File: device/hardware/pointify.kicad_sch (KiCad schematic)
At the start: 14 parts, among them J1 USB_C, J2 SWIO, J3 GND, J4 PWM1, J5 PWM2, U1 CH32X033F8P6

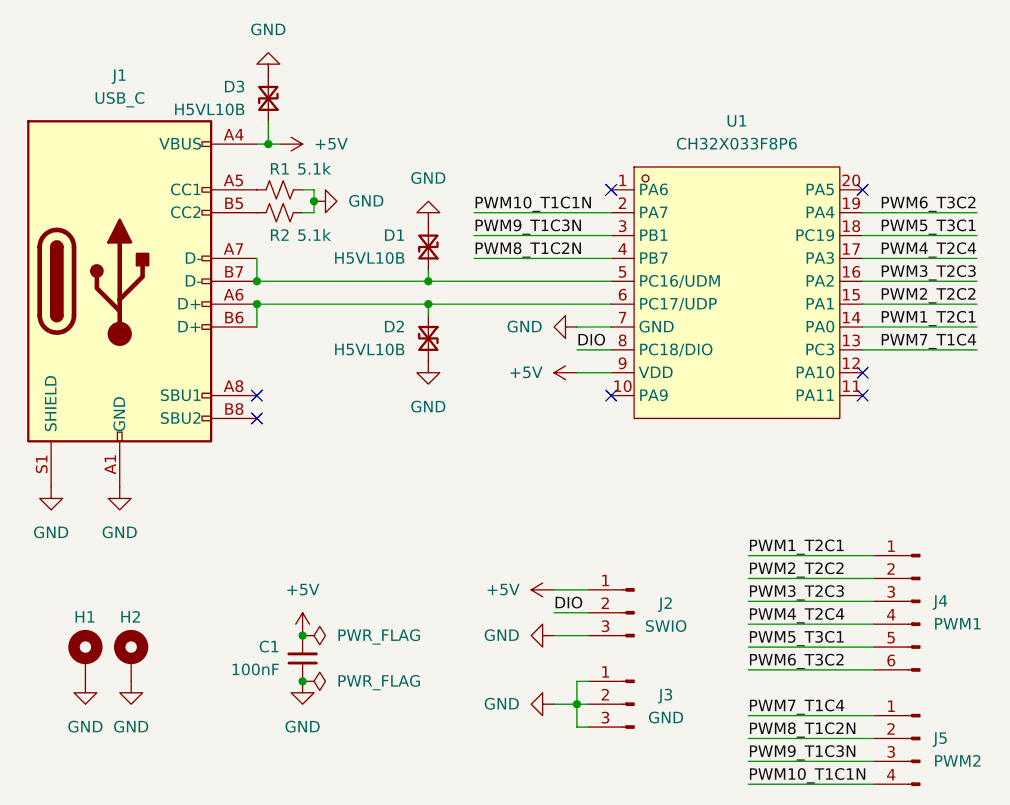
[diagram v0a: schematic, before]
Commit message: pcb v2.1: fix pinmaps
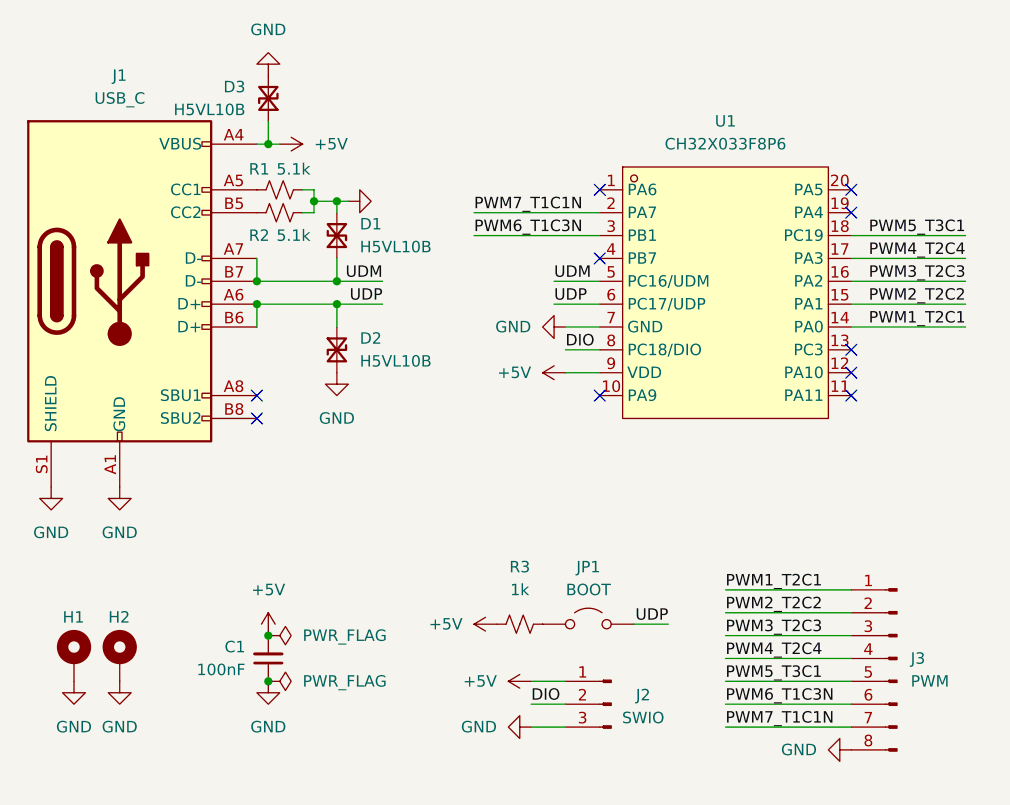
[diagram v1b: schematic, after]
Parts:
- removed J3: GND, Connector_PinHeader_2.54mm:PinHeader_1x03_P2.54mm_Vertical, symbol Connector:Conn_01x03_Pin
- removed J5: PWM2, Connector_PinHeader_2.00mm:PinHeader_1x04_P2.00mm_Vertical, symbol Connector:Conn_01x04_Pin
- added JP1: BOOT, Connector_PinHeader_2.54mm:PinHeader_1x02_P2.54mm_Vertical, symbol Jumper:Jumper_2_Open
- added R3: 1k, Resistor_SMD:R_0402_1005Metric_Pad0.72x0.64mm_HandSolder, symbol Device:R_Small_US
- J3: renamed from J4; value PWM1 -> PWM; footprint Connector_PinHeader_2.54mm:PinHeader_1x06_P2.54mm_Vertical -> Connector_PinHeader_2.54mm:PinHeader_1x08_P2.54mm_Vertical; symbol Connector:Conn_01x06_Pin -> Connector:Conn_01x08_Pin
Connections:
- net +5V: now also R3.1
- net GND: now also J3.8 (Pin_8)
- net UDP: now reaches D2.1 (A1), J1.A6 (D+), J1.B6 (D+), U1.6 (PC17/UDP)
- net UDP: now also JP1.2 (B)
- net UDM: now reaches D1.1 (A1), J1.A7 (D-), J1.B7 (D-), U1.5 (PC16/UDM)
- net PWM10_T1C1N renamed PWM7_T1C1N
- net PWM7_T1C1N: now also J3.7 (Pin_7)
- net PWM6_T3C2: no longer names the net of U1.19 (PA4)
- net PWM6_T3C2: no longer J3.6 (Pin_6)
- net PWM7_T1C4: no longer names the net of U1.13 (PC3)
- net PWM8_T1C2N: no longer names the net of U1.4 (PB7)
- net PWM9_T1C3N renamed PWM6_T1C3N
- net PWM6_T1C3N: now also J3.6 (Pin_6)
- new net: JP1.1 (A), R3.2
- no-connect marks 7 -> 10
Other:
- moved on the sheet: C1, D1, D2, H1, H2, J2, U1

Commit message: add: release workflows
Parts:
- H1, H2: now in the parts list
- J2, J3, JP1: now left out of the parts list
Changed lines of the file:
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@@
 		(unit 1)
 		(exclude_from_sim no)
-		(in_bom yes)
+		(in_bom no)
 		(on_board yes)
 		(dnp no)
@@
 		(unit 1)
 		(exclude_from_sim no)
-		(in_bom no)
+		(in_bom yes)
 		(on_board yes)
 		(dnp no)
@@
 		(unit 1)
 		(exclude_from_sim no)
-		(in_bom yes)
+		(in_bom no)
 		(on_board yes)
 		(dnp no)
@@
 		(unit 1)
 		(exclude_from_sim no)
-		(in_bom yes)
+		(in_bom no)
 		(on_board yes)
 		(dnp no)
@@
 		(unit 1)
 		(exclude_from_sim no)
-		(in_bom no)
-		(on_board yes)
-		(dnp no)
+		(in_bom yes)
+		(on_board yes)
+		(dnp no)

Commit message: update: pcb v2.2
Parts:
- removed D1, D2, D3: H5VL10B, Diode_SMD:D_SOD-882, symbol Device:D_TVS_Small
- removed J2: SWIO, Connector_PinHeader_2.54mm:PinHeader_1x03_P2.54mm_Vertical, symbol Connector:Conn_01x03_Pin
- added C2: 1uF, Capacitor_SMD:C_0402_1005Metric, symbol Device:C_Small
- C1: footprint Capacitor_SMD:C_0402_1005Metric_Pad0.74x0.62mm_HandSolder -> Capacitor_SMD:C_0402_1005Metric
- JP1: footprint Connector_PinHeader_2.54mm:PinHeader_1x02_P2.54mm_Vertical -> Connector_PinHeader_2.00mm:PinHeader_1x02_P2.00mm_Vertical
- R1, R2, R3: footprint Resistor_SMD:R_0402_1005Metric_Pad0.72x0.64mm_HandSolder -> Resistor_SMD:R_0402_1005Metric
- U1: footprint ch32x033f8p6:CH32X033F8P6 -> Package_SO:TSSOP-20_4.4x6.5mm_P0.65mm
- renumbered J3 to J2
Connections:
- net +5V: now also C2.2
- net GND: now also J2.1 (Pin_1), C2.1; no longer J2.8 (Pin_8)
- net PWM4_T2C4: now also J2.5 (Pin_5); no longer J2.4 (Pin_4)
- net DIO: no longer names the net of U1.8 (PC18/DIO)
- net PWM1_T2C1 renamed PWM7_T2C1
- net PWM7_T2C1: now also J2.8 (Pin_8); no longer J2.1 (Pin_1)
- net PWM2_T2C2 renamed PWM1_T1C1N
- net PWM1_T1C1N: now also U1.2 (PA7); no longer U1.15 (PA1)
- net PWM3_T2C3 renamed PWM2_T1C3N
- net PWM2_T1C3N: now also U1.3 (PB1); no longer U1.16 (PA2)
- net PWM5_T3C1 renamed PWM3_T3C1
- net PWM3_T3C1: now also J2.4 (Pin_4); no longer J2.5 (Pin_5)
- net PWM6_T1C3N renamed PWM5_T2C3
- net PWM5_T2C3: now also U1.16 (PA2); no longer U1.3 (PB1)
- net PWM7_T1C1N renamed PWM6_T2C2
- net PWM6_T2C2: now also U1.15 (PA1); no longer U1.2 (PA7)
- no-connect marks 10 -> 11
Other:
- moved on the sheet: C1, H1, H2, J2, JP1, R3, U1

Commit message: update: pcb v2.3 with PWM8
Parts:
- J2: footprint Connector_PinHeader_2.54mm:PinHeader_1x08_P2.54mm_Vertical -> Connector_PinHeader_2.54mm:PinHeader_1x09_P2.54mm_Vertical; symbol Connector:Conn_01x08_Pin -> Connector:Conn_01x09_Pin; now in the parts list
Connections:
- net PWM8_T3C2: now reaches U1.8 (PC18/DIO)
- net PWM8_T3C2: now also J2.9 (Pin_9)
- no-connect marks 11 -> 10
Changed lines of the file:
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@@
 		(at 157.48 86.36)
 	)
-	(no_connect
-		(at 157.48 96.52)
-	)
 	(wire
 		(pts
@@
 	(wire
 		(pts
+			(xy 143.51 96.52) (xy 157.48 96.52)
+		)
+		(stroke
+			(width 0)
+			(type default)
+		)
+	)
+	(wire
+		(pts
 			(xy 185.42 88.9) (xy 198.12 88.9)
 		)
@@
 		(pts
 			(xy 172.72 121.92) (xy 186.69 121.92)
+		)
+		(stroke
+			(width 0)
+			(type default)
+		)
+	)
+	(wire
+		(pts
+			(xy 172.72 142.24) (xy 186.69 142.24)
 		)
 		(stroke
@@
 		)
 	)
+	(label "PWM8_T3C2"
+		(at 143.51 96.52 0)
+		(effects
+			(font
+				(size 1.27 1.27)
+			)
+			(justify left bottom)
+		)
+	)
 	(label "PWM3_T3C1"
 		(at 198.12 83.82 180)
@@
 		)
 	)
+	(label "PWM8_T3C2"
+		(at 172.72 142.24 0)
+		(effects
+			(font
+				(size 1.27 1.27)
+			)
+			(justify left bottom)
+		)
+	)
 	(label "PWM6_T2C2"
 		(at 172.72 137.16 0)
@@
 		)
 		(instances
-			(project ""
+			(project "pointify"
 				(path "/4afa4f1a-2340-42a5-ad22-9ab0d7448eb2"
 					(reference "#PWR05")
@@
 		)
 		(instances
-			(project ""
+			(project "pointify"
 				(path "/4afa4f1a-2340-42a5-ad22-9ab0d7448eb2"
 					(reference "#PWR01")
@@
 		)
 		(instances
-			(project ""
+			(project "pointify"
 				(path "/4afa4f1a-2340-42a5-ad22-9ab0d7448eb2"
 					(reference "JP1")
@@
 		)
 		(instances
-			(project ""
+			(project "pointify"
 				(path "/4afa4f1a-2340-42a5-ad22-9ab0d7448eb2"
 					(reference "R1")
@@
 	)
 	(symbol
-		(lib_id "Connector:Conn_01x08_Pin")
-		(at 191.77 129.54 0)
+		(lib_id "Connector:Conn_01x09_Pin")
+		(at 191.77 132.08 0)
 		(mirror y)
 		(unit 1)
 		(exclude_from_sim no)
-		(in_bom no)
+		(in_bom yes)
 		(on_board yes)
 		(dnp no)
 		(property "Reference" "J2"
-			(at 193.294 129.54 0)
+			(at 193.294 132.08 0)
 			(effects
 				(font
@@
 		)
 		(property "Value" "PWM"
-			(at 193.294 132.08 0)
+			(at 193.294 134.62 0)
 			(effects
 				(font
@@
 			)
 		)
-		(property "Footprint" "Connector_PinHeader_2.54mm:PinHeader_1x08_P2.54mm_Vertical"
-			(at 191.77 129.54 0)
+		(property "Footprint" "Connector_PinHeader_2.54mm:PinHeader_1x09_P2.54mm_Vertical"
+			(at 191.77 132.08 0)
 			(effects
 				(font
@@
 		)
 		(property "Datasheet" "~"
-			(at 191.77 129.54 0)
-			(effects
-				(font
-					(size 1.27 1.27)
-				)
-				(hide yes)
-			)
-		)
-		(property "Description" "Generic connector, single row, 01x08, script generated"
-			(at 191.77 129.54 0)
+			(at 191.77 132.08 0)
+			(effects
+				(font
+					(size 1.27 1.27)
+				)
+				(hide yes)
+			)
+		)
+		(property "Description" "Generic connector, single row, 01x09, script generated"
+			(at 191.77 132.08 0)
 			(effects
 				(font
@@
 		)
 		(pin "8"
+		)
+		(pin "9"
 		)
 		(instances
@@
 		)
 		(instances
-			(project ""
+			(project "pointify"
 				(path "/4afa4f1a-2340-42a5-ad22-9ab0d7448eb2"
 					(reference "J1")
@@
 				)
 				(justify right)
+				(hide yes)
 			)
 		)
@@
 		)
 		(instances
-			(project ""
+			(project "pointify"
 				(path "/4afa4f1a-2340-42a5-ad22-9ab0d7448eb2"
 					(reference "H1")
@@
 		)
 		(instances
-			(project ""
+			(project "pointify"
 				(path "/4afa4f1a-2340-42a5-ad22-9ab0d7448eb2"
 					(reference "R3")
